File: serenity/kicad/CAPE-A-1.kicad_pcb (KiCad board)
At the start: 4 copper layers, 55 x 35 mm, 25 parts, among them J1 PB2I-P1-2x18, J10 Nano-Fit-4P-POWER, J2 PB2I-P2-2x18, J3 JST-GH-4P-CAN, J4 JST-GH-4P-RS485, J5 JST-GH-4P-1553, J6 JST-GH-6P-ETH1, J7 JST-GH-6P-ETH2, J8 JST-GH-3P-ESC-TELEM, J9 1x8-SERVO-PWM, T1 SM-1553-11, U1 ICM-42688-P, U10 SLB9670, U2 BMP388, U3 SAM-M10Q-00B, U4 ATA6561, U5 MAX3485E, U6 DS26LV31, U7 DS26LV32, U8 DP83825I, U9 DP83825I

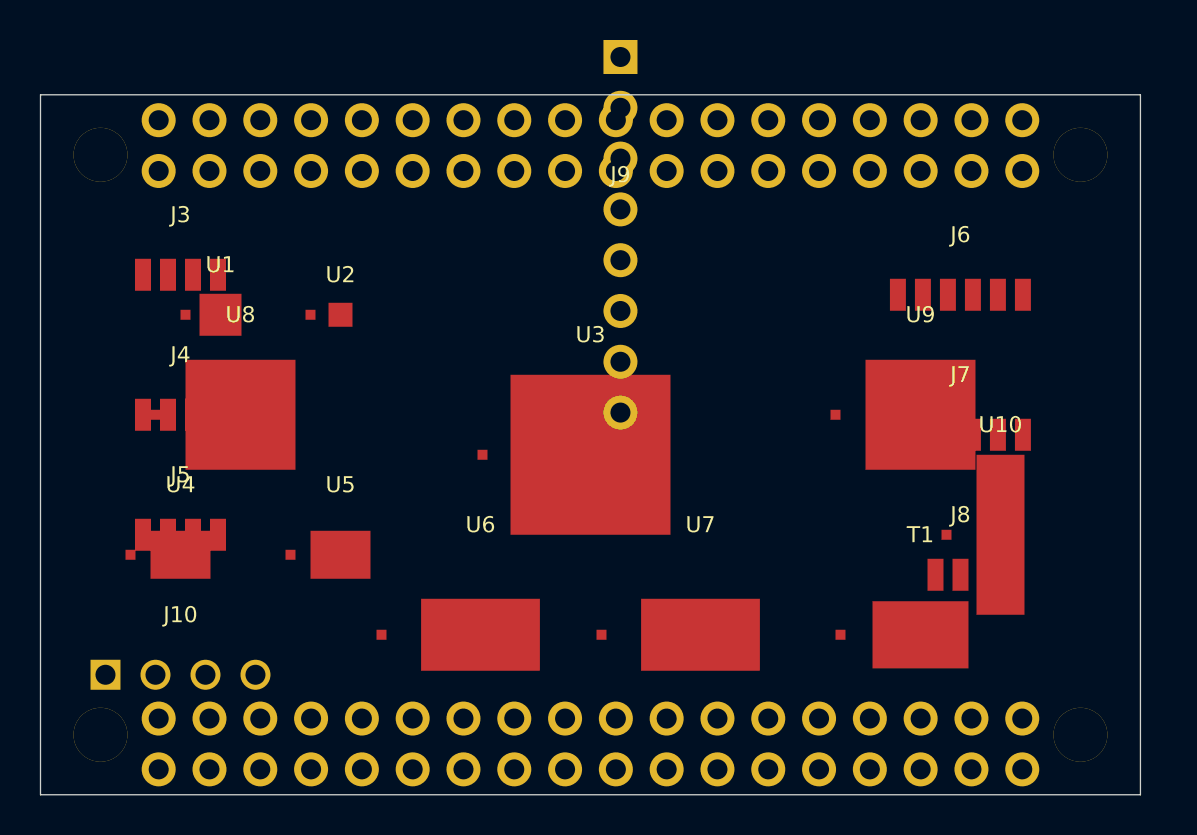
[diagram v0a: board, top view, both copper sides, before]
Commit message: Replace generic PCB silk labels with short descriptive names
Update all F.SilkS/B.SilkS fp_text reference labels across 7 KiCad PCB
files, replacing J/U/T numeric designators with function-based names so
each component is identifiable on the board without a BOM lookup.

CAPE-A-1 / CAPE-A-1-no-comment:
  J1→PB2-P1, J2→PB2-P2, U1→IMU, U2→BARO, U3→GPS,
  U4/U5→CAN-TR/RS485, U6→1553-DRV, U7→1553-RCV, T1→1553-XFM,
  U8/U9→ETH1-PHY/ETH2-PHY, U10→TPM,
  J3→CAN-FD, J4→RS-485, J5→MIL-1553, J6→ETH1, J7→ETH2,
  J8→ESC-TLM, J9→SERVO, J10→PWR-IN

CAPE-B-1 (adds RF + payload peripherals):
  U1→LORA, U2→WIFI-BT, U10→SD-WB, U11→NOR-FLASH,
  U12→WINCH-DRV, U13→LOAD-ADC, U14→PWM-I2C,
  J8→SIK-TLM, J9→RC-RCVR, J11→WINCH, J12→LOAD-CELL, J13→NAV-LIGHT

COMMS-HAT-1 (connectors + crystal only; ICs already descriptive):
  J1→SIK-UART, J2→ETH, J3→GPIO-EXT, J4→CAN-FD,
  JP4→PWR-IN, Y1→ETH-CLK

COMMS-HAT-SWITCH:
  Y1→SW-CLK

TRIHAT-1 (superseded; ICs + inferred connector mapping):
  U1→IMU, U2→BARO, U3→GPS, U4→CAN-CTRL, U5→CAN-TR,
  U6→ETH-CTRL, U7→ETH-MAG, U8→TPM, U9→LDO, Y1→ETH-CLK,
  J-connectors mapped from net list (GPS/CAN-FD/ETH/ESC-OUT/SERVO-OUT/etc.)

CM3-CARRIER-1:
  J1→CM3-SDIMM, U1→CAN-CTRL, U1B→CAN-TR, U2→RS485,
  U3→MIL-1553, U4→ETH-CTRL, U5→USB-UART, U6→LDO, U7→HAT-EEPROM

Boards already fully descriptive (SENSORHAT-1, CM4-CARRIER-1,
CM4-CARRIER-2) are unchanged.

https://claude.ai/code/session_01GniMw4QukTVM7JMzyVjH6p
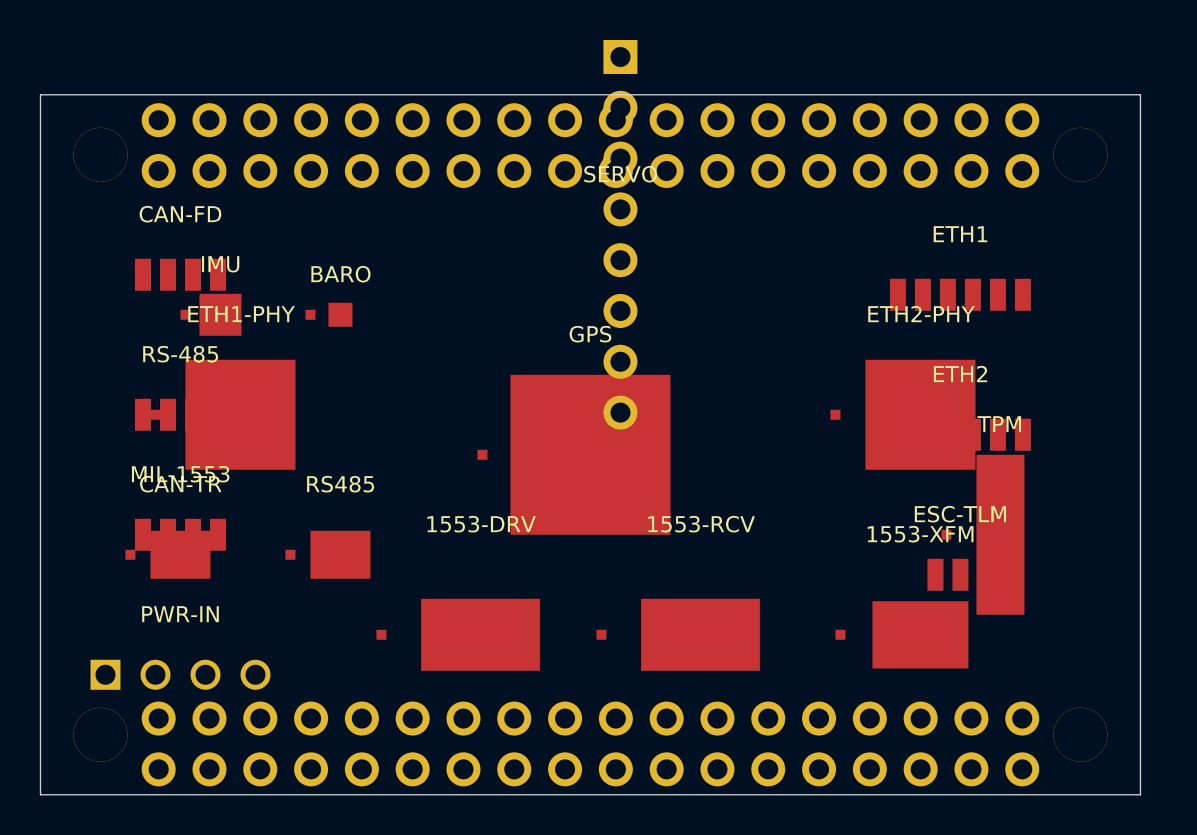
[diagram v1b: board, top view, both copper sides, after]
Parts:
- removed J1: PB2I-P1-2x18, PocketBeagle2:2x18_P1_Socket
- removed J10: Nano-Fit-4P-POWER, Connector_Molex_NanoFit
- removed J2: PB2I-P2-2x18, PocketBeagle2:2x18_P2_Socket
- removed J3: JST-GH-4P-CAN, JST_GH_4P
- removed J4: JST-GH-4P-RS485, JST_GH_4P
- removed J5: JST-GH-4P-1553, JST_GH_4P
- removed J6: JST-GH-6P-ETH1, JST_GH_6P
- removed J7: JST-GH-6P-ETH2, JST_GH_6P
- removed J8: JST-GH-3P-ESC-TELEM, JST_GH_3P
- removed J9: 1x8-SERVO-PWM, Connector_PinHeader_2.54mm
- removed T1: SM-1553-11, Package
- removed U1: ICM-42688-P, Package
- removed U10: SLB9670, Package
- removed U2: BMP388, Package
- removed U3: SAM-M10Q-00B, Package
- removed U4: ATA6561, Package
- removed U5: MAX3485E, Package
- removed U6: DS26LV31, Package
- removed U7: DS26LV32, Package
- removed U8, U9: DP83825I, Package
- added 1553-DRV: DS26LV31, Package, F.Cu at (143.0, 114.5)
- added 1553-RCV: DS26LV32, Package, F.Cu at (154.0, 114.5)
- added 1553-XFM: SM-1553-11, Package, F.Cu at (165.0, 114.5)
- added BARO: BMP388, Package, F.Cu at (136.0, 98.5)
- added CAN-FD: JST-GH-4P-CAN, JST_GH_4P, F.Cu at (128.0, 96.5)
- added CAN-TR: ATA6561, Package, F.Cu at (128.0, 110.5)
- added ESC-TLM: JST-GH-3P-ESC-TELEM, JST_GH_3P, F.Cu at (167.0, 111.5)
- added ETH1: JST-GH-6P-ETH1, JST_GH_6P, F.Cu at (167.0, 97.5)
- added ETH1-PHY: DP83825I, Package, F.Cu at (131.0, 103.5)
- added ETH2: JST-GH-6P-ETH2, JST_GH_6P, F.Cu at (167.0, 104.5)
- added ETH2-PHY: DP83825I, Package, F.Cu at (165.0, 103.5)
- added GPS: SAM-M10Q-00B, Package, F.Cu at (148.5, 105.5)
- added IMU: ICM-42688-P, Package, F.Cu at (130.0, 98.5)
- added MIL-1553: JST-GH-4P-1553, JST_GH_4P, F.Cu at (128.0, 109.5)
- added PB2-P1: PB2I-P1-2x18, PocketBeagle2:2x18_P1_Socket, B.Cu at (148.5, 90.0)
- added PB2-P2: PB2I-P2-2x18, PocketBeagle2:2x18_P2_Socket, B.Cu at (148.5, 120.0)
- added PWR-IN: Nano-Fit-4P-POWER, Connector_Molex_NanoFit, F.Cu at (128.0, 116.5)
- added RS-485: JST-GH-4P-RS485, JST_GH_4P, F.Cu at (128.0, 103.5)
- added RS485: MAX3485E, Package, F.Cu at (136.0, 110.5)
- added SERVO: 1x8-SERVO-PWM, Connector_PinHeader_2.54mm, F.Cu at (150.0, 94.5)
- added TPM: SLB9670, Package, F.Cu at (169.0, 109.5)
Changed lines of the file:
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@@
     (pad "" thru_hole circle (at 0 0) (size 2.7 2.7) (drill 2.7) (layers "*.Cu" "*.Mask")))
   (footprint "PocketBeagle2:2x18_P1_Socket" (layer "B.Cu") (at 148.5 90.04) (property "Description" "PocketBeagle 2 Industrial P1 socket 2x18 2.54mm TH — verify pin mapping from AM6254 schematic")
-    (fp_text reference "J1" (at 0 -4) (layer "B.SilkS")
+    (fp_text reference "PB2-P1" (at 0 -4) (layer "B.SilkS")
       (effects (font (size 1 1) (thickness 0.15)) (justify mirror)))
     (fp_text value "PB2I-P1-2x18" (at 0 5) (layer "B.Fab")
@@
     (pad "36" thru_hole circle (at 21.59 1.27) (size 1.7 1.7) (drill 1.0) (layers "*.Cu" "*.Mask")))
   (footprint "PocketBeagle2:2x18_P2_Socket" (layer "B.Cu") (at 148.5 119.96) (property "Description" "PocketBeagle 2 Industrial P2 socket 2x18 2.54mm TH — verify pin mapping from AM6254 schematic")
-    (fp_text reference "J2" (at 0 -4) (layer "B.SilkS")
+    (fp_text reference "PB2-P2" (at 0 -4) (layer "B.SilkS")
       (effects (font (size 1 1) (thickness 0.15)) (justify mirror)))
     (fp_text value "PB2I-P2-2x18" (at 0 5) (layer "B.Fab")
@@
     (pad "36" thru_hole circle (at 21.59 1.27) (size 1.7 1.7) (drill 1.0) (layers "*.Cu" "*.Mask")))
   (footprint "Package" (layer "F.Cu") (at 130 98.5) (property "Description" "TDK InvenSense ICM-42688-P 6DOF IMU LGA-14 2.7x2.7mm")
-    (fp_text reference "U1" (at 0 -2.5) (layer "F.SilkS")
+    (fp_text reference "IMU" (at 0 -2.5) (layer "F.SilkS")
       (effects (font (size 0.8 0.8) (thickness 0.15))))
     (fp_text value "ICM-42688-P" (at 0 2.5) (layer "F.Fab")
@@
     (pad "EP" smd rect (at 0 0) (size 2.10 2.10) (layers "F.Cu" "F.Paste" "F.Mask")))
   (footprint "Package" (layer "F.Cu") (at 136 98.5) (property "Description" "Bosch BMP388 barometric pressure sensor LGA-8 2.0x2.0mm")
-    (fp_text reference "U2" (at 0 -2.0) (layer "F.SilkS")
+    (fp_text reference "BARO" (at 0 -2.0) (layer "F.SilkS")
       (effects (font (size 0.8 0.8) (thickness 0.15))))
     (fp_text value "BMP388" (at 0 2.0) (layer "F.Fab")
@@
     (pad "EP" smd rect (at 0 0) (size 1.20 1.20) (layers "F.Cu" "F.Paste" "F.Mask")))
   (footprint "Package" (layer "F.Cu") (at 148.5 105.5) (property "Description" "u-blox SAM-M10Q-00B GPS/GNSS module 9.6x9.6mm — verify pinout from datasheet")
-    (fp_text reference "U3" (at 0 -6.0) (layer "F.SilkS")
+    (fp_text reference "GPS" (at 0 -6.0) (layer "F.SilkS")
       (effects (font (size 0.8 0.8) (thickness 0.15))))
     (fp_text value "SAM-M10Q-00B" (at 0 6.0) (layer "F.Fab")
@@
     (pad "EP" smd rect (at 0 0) (size 8.00 8.00) (layers "F.Cu" "F.Paste" "F.Mask")))
   (footprint "Package" (layer "F.Cu") (at 128 110.5) (property "Description" "Microchip ATA6561 CAN FD transceiver SOIC-8")
-    (fp_text reference "U4" (at 0 -3.5) (layer "F.SilkS")
+    (fp_text reference "CAN-TR" (at 0 -3.5) (layer "F.SilkS")
       (effects (font (size 0.8 0.8) (thickness 0.15))))
     (fp_text value "ATA6561" (at 0 3.5) (layer "F.Fab")
@@
     (pad "EP" smd rect (at 0 0) (size 3.00 2.40) (layers "F.Cu" "F.Paste" "F.Mask")))
   (footprint "Package" (layer "F.Cu") (at 136 110.5) (property "Description" "Maxim MAX3485E RS-485 half-duplex transceiver SOIC-8")
-    (fp_text reference "U5" (at 0 -3.5) (layer "F.SilkS")
+    (fp_text reference "RS485" (at 0 -3.5) (layer "F.SilkS")
       (effects (font (size 0.8 0.8) (thickness 0.15))))
     (fp_text value "MAX3485E" (at 0 3.5) (layer "F.Fab")
@@
     (pad "EP" smd rect (at 0 0) (size 3.00 2.40) (layers "F.Cu" "F.Paste" "F.Mask")))
   (footprint "Package" (layer "F.Cu") (at 143 114.5) (property "Description" "TI DS26LV31 quad LVDS 1553 line driver SOIC-16")
-    (fp_text reference "U6" (at 0 -5.5) (layer "F.SilkS")
+    (fp_text reference "1553-DRV" (at 0 -5.5) (layer "F.SilkS")
       (effects (font (size 0.8 0.8) (thickness 0.15))))
     (fp_text value "DS26LV31" (at 0 5.5) (layer "F.Fab")
@@
     (pad "EP" smd rect (at 0 0) (size 5.94 3.60) (layers "F.Cu" "F.Paste" "F.Mask")))
   (footprint "Package" (layer "F.Cu") (at 154 114.5) (property "Description" "TI DS26LV32 quad LVDS 1553 line receiver SOIC-16")
-    (fp_text reference "U7" (at 0 -5.5) (layer "F.SilkS")
+    (fp_text reference "1553-RCV" (at 0 -5.5) (layer "F.SilkS")
       (effects (font (size 0.8 0.8) (thickness 0.15))))
     (fp_text value "DS26LV32" (at 0 5.5) (layer "F.Fab")
@@
     (pad "EP" smd rect (at 0 0) (size 5.94 3.60) (layers "F.Cu" "F.Paste" "F.Mask")))
   (footprint "Package" (layer "F.Cu") (at 165 114.5) (property "Description" "Halo SM-1553-11 MIL-STD-1553 isolation transformer 4.8x8.0mm")
-    (fp_text reference "T1" (at 0 -5.0) (layer "F.SilkS")
+    (fp_text reference "1553-XFM" (at 0 -5.0) (layer "F.SilkS")
       (effects (font (size 0.8 0.8) (thickness 0.15))))
     (fp_text value "SM-1553-11" (at 0 5.0) (layer "F.Fab")
@@
     (pad "EP" smd rect (at 0 0) (size 4.80 3.36) (layers "F.Cu" "F.Paste" "F.Mask")))
   (footprint "Package" (layer "F.Cu") (at 131 103.5) (property "Description" "TI DP83825I 100Mbps RMII Ethernet PHY LQFP-48 7x7mm")
-    (fp_text reference "U8" (at 0 -5.0) (layer "F.SilkS")
+    (fp_text reference "ETH1-PHY" (at 0 -5.0) (layer "F.SilkS")
       (effects (font (size 0.8 0.8) (thickness 0.15))))
     (fp_text value "DP83825I" (at 0 5.0) (layer "F.Fab")
@@
     (pad "EP" smd rect (at 0 0) (size 5.50 5.50) (layers "F.Cu" "F.Paste" "F.Mask")))
   (footprint "Package" (layer "F.Cu") (at 165 103.5) (property "Description" "TI DP83825I 100Mbps RMII Ethernet PHY LQFP-48 7x7mm")
-    (fp_text reference "U9" (at 0 -5.0) (layer "F.SilkS")
+    (fp_text reference "ETH2-PHY" (at 0 -5.0) (layer "F.SilkS")
       (effects (font (size 0.8 0.8) (thickness 0.15))))
     (fp_text value "DP83825I" (at 0 5.0) (layer "F.Fab")
@@
     (pad "EP" smd rect (at 0 0) (size 5.50 5.50) (layers "F.Cu" "F.Paste" "F.Mask")))
   (footprint "Package" (layer "F.Cu") (at 169 109.5) (property "Description" "Infineon SLB9670 TPM 2.0 SPI TSSOP-28 9.7x4.4mm")
-    (fp_text reference "U10" (at 0 -5.5) (layer "F.SilkS")
+    (fp_text reference "TPM" (at 0 -5.5) (layer "F.SilkS")
       (effects (font (size 0.8 0.8) (thickness 0.15))))
     (fp_text value "SLB9670" (at 0 5.5) (layer "F.Fab")
@@
     (pad "EP" smd rect (at 0 0) (size 2.40 8.00) (layers "F.Cu" "F.Paste" "F.Mask")))
   (footprint "JST_GH_4P" (layer "F.Cu") (at 128 96.5) (property "Description" "CAN FD external connector — GND CAN_H CAN_L +3V3")
-    (fp_text reference "J3" (at 0 -3) (layer "F.SilkS")
+    (fp_text reference "CAN-FD" (at 0 -3) (layer "F.SilkS")
       (effects (font (size 0.8 0.8) (thickness 0.15))))
     (fp_text value "JST-GH-4P-CAN" (at 0 3) (layer "F.Fab")
@@
     (pad "4" smd rect (at 1.875 0) (size 0.8 1.6) (layers "F.Cu" "F.Paste" "F.Mask")))
   (footprint "JST_GH_4P" (layer "F.Cu") (at 128 103.5) (property "Description" "RS-485 external connector — GND RS485_A RS485_B +3V3")
-    (fp_text reference "J4" (at 0 -3) (layer "F.SilkS")
+    (fp_text reference "RS-485" (at 0 -3) (layer "F.SilkS")
       (effects (font (size 0.8 0.8) (thickness 0.15))))
     (fp_text value "JST-GH-4P-RS485" (at 0 3) (layer "F.Fab")
@@
     (pad "4" smd rect (at 1.875 0) (size 0.8 1.6) (layers "F.Cu" "F.Paste" "F.Mask")))
   (footprint "JST_GH_4P" (layer "F.Cu") (at 128 109.5) (property "Description" "MIL-STD-1553 bus external connector — GND BUS_1553_A_P BUS_1553_A_N GND")
-    (fp_text reference "J5" (at 0 -3) (layer "F.SilkS")
+    (fp_text reference "MIL-1553" (at 0 -3) (layer "F.SilkS")
       (effects (font (size 0.8 0.8) (thickness 0.15))))
     (fp_text value "JST-GH-4P-1553" (at 0 3) (layer "F.Fab")
@@
     (pad "4" smd rect (at 1.875 0) (size 0.8 1.6) (layers "F.Cu" "F.Paste" "F.Mask")))
   (footprint "JST_GH_6P" (layer "F.Cu") (at 167 97.5) (property "Description" "Ethernet 1 MagJack — ETH1_TX_P ETH1_TX_N GND GND ETH1_RX_P ETH1_RX_N")
-    (fp_text reference "J6" (at 0 -3) (layer "F.SilkS")
+    (fp_text reference "ETH1" (at 0 -3) (layer "F.SilkS")
       (effects (font (size 0.8 0.8) (thickness 0.15))))
     (fp_text value "JST-GH-6P-ETH1" (at 0 3) (layer "F.Fab")
@@
     (pad "6" smd rect (at 3.125 0) (size 0.8 1.6) (layers "F.Cu" "F.Paste" "F.Mask")))
   (footprint "JST_GH_6P" (layer "F.Cu") (at 167 104.5) (property "Description" "Ethernet 2 MagJack — ETH2_TX_P ETH2_TX_N GND GND ETH2_RX_P ETH2_RX_N")
-    (fp_text reference "J7" (at 0 -3) (layer "F.SilkS")
+    (fp_text reference "ETH2" (at 0 -3) (layer "F.SilkS")
       (effects (font (size 0.8 0.8) (thickness 0.15))))
     (fp_text value "JST-GH-6P-ETH2" (at 0 3) (layer "F.Fab")
@@
     (pad "6" smd rect (at 3.125 0) (size 0.8 1.6) (layers "F.Cu" "F.Paste" "F.Mask")))
   (footprint "JST_GH_3P" (layer "F.Cu") (at 167 111.5) (property "Description" "ESC telemetry UART — GND UART_ESC_TX UART_ESC_RX")
-    (fp_text reference "J8" (at 0 -3) (layer "F.SilkS")
+    (fp_text reference "ESC-TLM" (at 0 -3) (layer "F.SilkS")
       (effects (font (size 0.8 0.8) (thickness 0.15))))
     (fp_text value "JST-GH-3P-ESC-TELEM" (at 0 3) (layer "F.Fab")
@@
     (pad "3" smd rect (at 1.25 0) (size 0.8 1.6) (layers "F.Cu" "F.Paste" "F.Mask")))
   (footprint "Connector_PinHeader_2.54mm" (layer "F.Cu") (at 150 94.5) (property "Description" "1x8 servo PWM header 2.54mm TH — SERVO0-SERVO7")
-    (fp_text reference "J9" (at 0 -3) (layer "F.SilkS")
+    (fp_text reference "SERVO" (at 0 -3) (layer "F.SilkS")
       (effects (font (size 0.8 0.8) (thickness 0.15))))
     (fp_text value "1x8-SERVO-PWM" (at 0 3) (layer "F.Fab")
@@
     (pad "8" thru_hole circle (at 0 8.89) (size 1.7 1.7) (drill 1.0) (layers "*.Cu" "*.Mask")))
   (footprint "Connector_Molex_NanoFit" (layer "F.Cu") (at 128 116.5) (property "Description" "Molex Nano-Fit 4-pin 5V power input — +5V +5V GND GND")
-    (fp_text reference "J10" (at 0 -3) (layer "F.SilkS")
+    (fp_text reference "PWR-IN" (at 0 -3) (layer "F.SilkS")
       (effects (font (size 0.8 0.8) (thickness 0.15))))
     (fp_text value "Nano-Fit-4P-POWER" (at 0 3) (layer "F.Fab")
